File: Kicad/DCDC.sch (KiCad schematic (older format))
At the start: 0 parts

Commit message: Agregado componente DC/DC
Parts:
- added IC1: MAX8881EUT33-T, symbol MAX8881EUT33-T
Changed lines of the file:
@@
 LIBS:batn
 LIBS:MCP73831
+LIBS:maxim
+LIBS:max8881
 LIBS:EMG-cache
-EELAYER 27 0
+EELAYER 25 0
 EELAYER END
 $Descr A4 11693 8268
@@
 Comment4 ""
 $EndDescr
+$Comp
+L MAX8881EUT33-T IC1
+U 1 1 57F2DBC0
+P 5200 3650
+F 0 "IC1" H 5050 4000 60  0000 C CNN
+F 1 "MAX8881EUT33-T" H 5200 4100 60  0000 C CNN
+F 2 "" H 5200 3650 60  0000 C CNN
+F 3 "" H 5200 3650 60  0000 C CNN
+	1    5200 3650
+	1    0    0    -1
+$EndComp
 $EndSCHEMATC

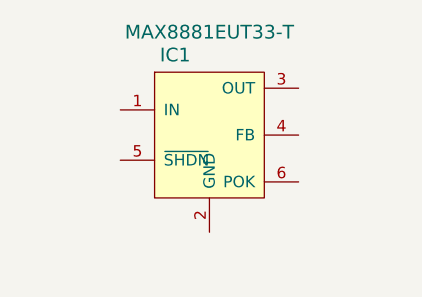
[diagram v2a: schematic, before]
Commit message: Circuito de cargador modificado. A los demás les agregué capacitor en la alimentación, pines sin conexión y cambié BATT- por GND
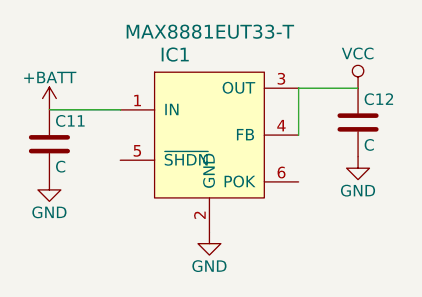
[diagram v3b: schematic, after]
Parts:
- added C11, C12: C, symbol C
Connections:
- net +BATT: now reaches IC1.1 (IN)
- net +BATT: now also C11.1
- net GND: now reaches IC1.2 (GND)
- net GND: now also C11.2, C12.2
- net VCC: now reaches IC1.3 (OUT)
- net VCC: now also IC1.4 (FB), C12.1
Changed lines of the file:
@@
 	1    0    0    -1
 $EndComp
+$Comp
+L GND #PWR17
+U 1 1 57FAED76
+P 5200 4075
+F 0 "#PWR17" H 5200 3825 50  0001 C CNN
+F 1 "GND" H 5200 3925 50  0000 C CNN
+F 2 "" H 5200 4075 50  0000 C CNN
+F 3 "" H 5200 4075 50  0000 C CNN
+	1    5200 4075
+	1    0    0    -1
+$EndComp
+Wire Wire Line
+	5590 3445 5590 3650
+$Comp
+L C C12
+U 1 1 57FAEFB7
+P 5850 3595
+F 0 "C12" H 5875 3695 50  0000 L CNN
+F 1 "C" H 5875 3495 50  0000 L CNN
+F 2 "" H 5888 3445 50  0000 C CNN
+F 3 "" H 5850 3595 50  0000 C CNN
+	1    5850 3595
+	1    0    0    -1
+$EndComp
+$Comp
+L GND #PWR19
+U 1 1 57FAF09C
+P 5850 3745
+F 0 "#PWR19" H 5850 3495 50  0001 C CNN
+F 1 "GND" H 5850 3595 50  0000 C CNN
+F 2 "" H 5850 3745 50  0000 C CNN
+F 3 "" H 5850 3745 50  0000 C CNN
+	1    5850 3745
+	1    0    0    -1
+$EndComp
+$Comp
+L VCC #PWR18
+U 1 1 57FAF102
+P 5850 3445
+F 0 "#PWR18" H 5850 3295 50  0001 C CNN
+F 1 "VCC" H 5850 3595 50  0000 C CNN
+F 2 "" H 5850 3445 50  0000 C CNN
+F 3 "" H 5850 3445 50  0000 C CNN
+	1    5850 3445
+	1    0    0    -1
+$EndComp
+Wire Wire Line
+	5590 3445 5850 3445
+$Comp
+L +BATT #PWR15
+U 1 1 57FAF186
+P 4500 3540
+F 0 "#PWR15" H 4500 3390 50  0001 C CNN
+F 1 "+BATT" H 4500 3680 50  0000 C CNN
+F 2 "" H 4500 3540 50  0000 C CNN
+F 3 "" H 4500 3540 50  0000 C CNN
+	1    4500 3540
+	1    0    0    -1
+$EndComp
+$Comp
+L C C11
+U 1 1 57FAF1C6
+P 4500 3690
+F 0 "C11" H 4525 3790 50  0000 L CNN
+F 1 "C" H 4525 3590 50  0000 L CNN
+F 2 "" H 4538 3540 50  0000 C CNN
+F 3 "" H 4500 3690 50  0000 C CNN
+	1    4500 3690
+	1    0    0    -1
+$EndComp
+$Comp
+L GND #PWR16
+U 1 1 57FAF245
+P 4500 3840
+F 0 "#PWR16" H 4500 3590 50  0001 C CNN
+F 1 "GND" H 4500 3690 50  0000 C CNN
+F 2 "" H 4500 3840 50  0000 C CNN
+F 3 "" H 4500 3840 50  0000 C CNN
+	1    4500 3840
+	1    0    0    -1
+$EndComp
+Wire Wire Line
+	4810 3540 4500 3540
 $EndSCHEMATC

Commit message: Agregados footprints y 3D de SOT23-6. Asociado componente IC1
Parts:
- IC1: footprint (none) -> EMG:sot23-6
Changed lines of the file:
@@
 F 0 "IC1" H 5050 4000 60  0000 C CNN
 F 1 "MAX8881EUT33-T" H 5200 4100 60  0000 C CNN
-F 2 "" H 5200 3650 60  0000 C CNN
+F 2 "EMG:sot23-6" H 5200 3650 60  0001 C CNN
 F 3 "" H 5200 3650 60  0000 C CNN
 	1    5200 3650
@@
 $EndComp
 $Comp
-L GND #PWR17
+L GND #PWR015
 U 1 1 57FAED76
 P 5200 4075
-F 0 "#PWR17" H 5200 3825 50  0001 C CNN
+F 0 "#PWR015" H 5200 3825 50  0001 C CNN
 F 1 "GND" H 5200 3925 50  0000 C CNN
 F 2 "" H 5200 4075 50  0000 C CNN
@@
 F 0 "C12" H 5875 3695 50  0000 L CNN
 F 1 "C" H 5875 3495 50  0000 L CNN
-F 2 "" H 5888 3445 50  0000 C CNN
+F 2 "" H 5888 3445 50  0001 C CNN
 F 3 "" H 5850 3595 50  0000 C CNN
 	1    5850 3595
@@
 $EndComp
 $Comp
-L GND #PWR19
+L GND #PWR016
 U 1 1 57FAF09C
 P 5850 3745
-F 0 "#PWR19" H 5850 3495 50  0001 C CNN
+F 0 "#PWR016" H 5850 3495 50  0001 C CNN
 F 1 "GND" H 5850 3595 50  0000 C CNN
 F 2 "" H 5850 3745 50  0000 C CNN
@@
 $EndComp
 $Comp
-L VCC #PWR18
+L VCC #PWR017
 U 1 1 57FAF102
 P 5850 3445
-F 0 "#PWR18" H 5850 3295 50  0001 C CNN
+F 0 "#PWR017" H 5850 3295 50  0001 C CNN
 F 1 "VCC" H 5850 3595 50  0000 C CNN
 F 2 "" H 5850 3445 50  0000 C CNN
@@
 	5590 3445 5850 3445
 $Comp
-L +BATT #PWR15
+L +BATT #PWR018
 U 1 1 57FAF186
 P 4500 3540
-F 0 "#PWR15" H 4500 3390 50  0001 C CNN
+F 0 "#PWR018" H 4500 3390 50  0001 C CNN
 F 1 "+BATT" H 4500 3680 50  0000 C CNN
 F 2 "" H 4500 3540 50  0000 C CNN
@@
 F 0 "C11" H 4525 3790 50  0000 L CNN
 F 1 "C" H 4525 3590 50  0000 L CNN
-F 2 "" H 4538 3540 50  0000 C CNN
+F 2 "" H 4538 3540 50  0001 C CNN
 F 3 "" H 4500 3690 50  0000 C CNN
 	1    4500 3690
@@
 $EndComp
 $Comp
-L GND #PWR16
+L GND #PWR019
 U 1 1 57FAF245
 P 4500 3840
-F 0 "#PWR16" H 4500 3590 50  0001 C CNN
+F 0 "#PWR019" H 4500 3590 50  0001 C CNN
 F 1 "GND" H 4500 3690 50  0000 C CNN
 F 2 "" H 4500 3840 50  0000 C CNN

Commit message: Agregados footprints de C_0805 y R_0805 y asociados a resistencias y capacitores del esquemático
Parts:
- C11, C12: footprint (none) -> EMG:C_0805
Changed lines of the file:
@@
 F 0 "C12" H 5875 3695 50  0000 L CNN
 F 1 "C" H 5875 3495 50  0000 L CNN
-F 2 "" H 5888 3445 50  0001 C CNN
+F 2 "EMG:C_0805" H 5888 3445 50  0001 C CNN
 F 3 "" H 5850 3595 50  0000 C CNN
 	1    5850 3595
@@
 F 0 "C11" H 4525 3790 50  0000 L CNN
 F 1 "C" H 4525 3590 50  0000 L CNN
-F 2 "" H 4538 3540 50  0001 C CNN
+F 2 "EMG:C_0805" H 4538 3540 50  0001 C CNN
 F 3 "" H 4500 3690 50  0000 C CNN
 	1    4500 3690
